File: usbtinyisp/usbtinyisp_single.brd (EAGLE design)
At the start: 44 x 36 mm, 27 parts, among them IC1 ATTINY2313-20P, IC2 74LVX125D, Q1 12000

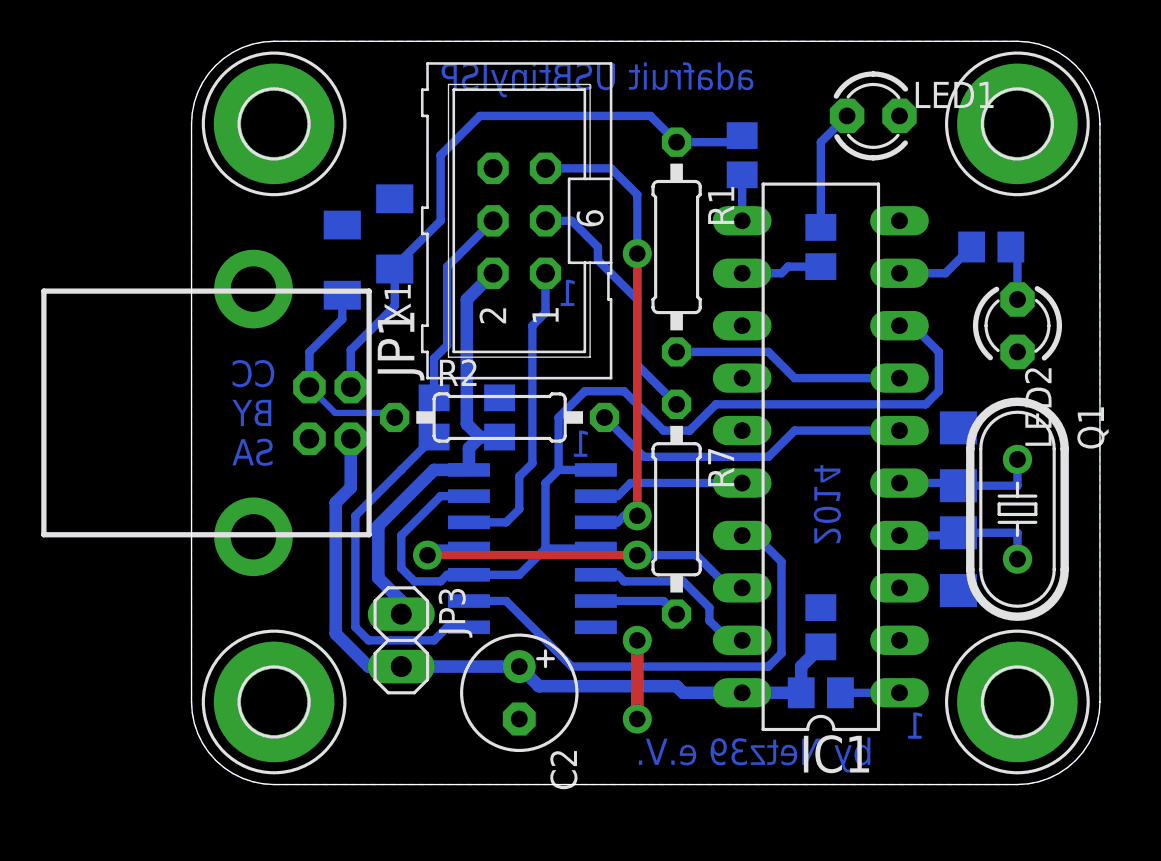
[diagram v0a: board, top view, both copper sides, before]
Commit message: add fuse and diode and route again the whole board
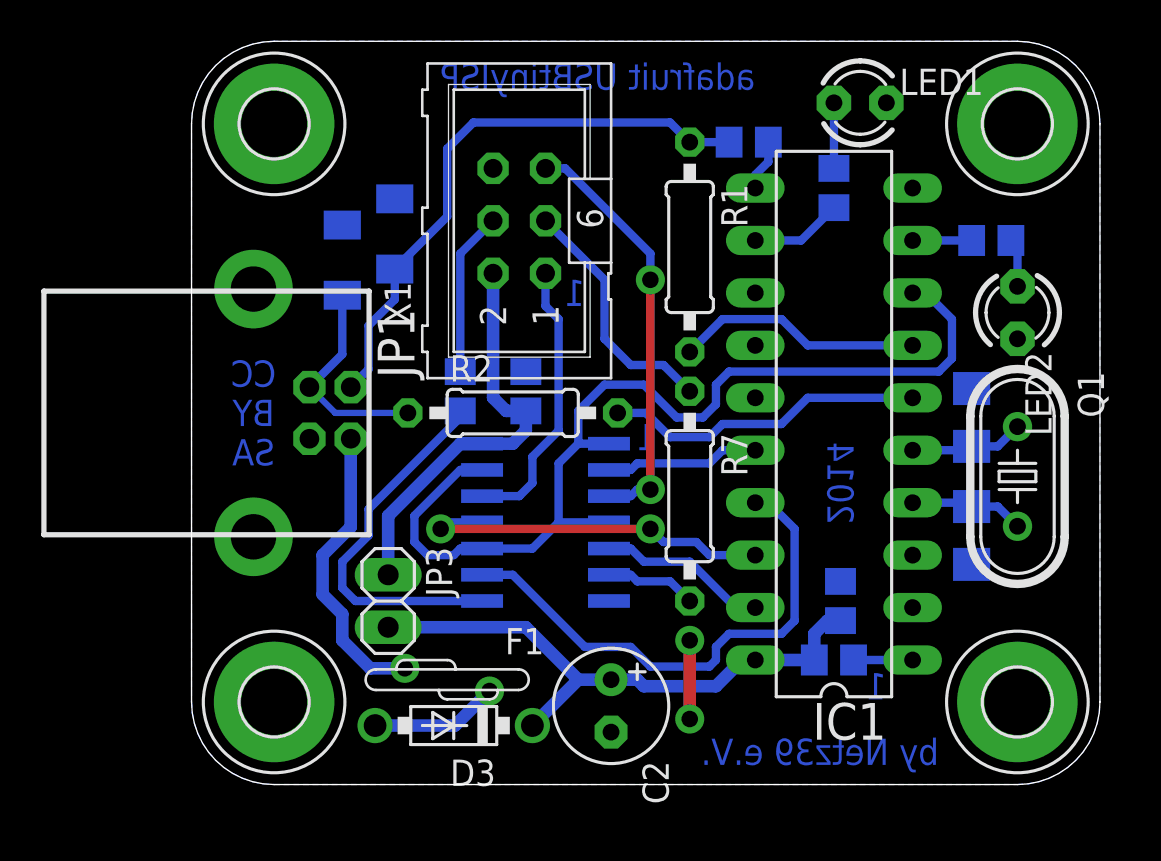
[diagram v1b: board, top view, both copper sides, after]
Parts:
- added D3: 1N5818-B, diode:DO41-7.6
- added F1: (no value), n39:LP60-050
- moved C2 4.49 mm to (20.3, 3.81)
- moved R6 2.93 mm to (31.1, 28.9)
- moved C4 2.01 mm to (37.8, 17.8)
- moved JP3 2.01 mm to (9.53, 8.89)
- moved C5 1.80 mm to (16.2, 19.1)
- moved R4 1.80 mm to (13.0, 19.1)
- moved R10 1.71 mm to (31.1, 6.03)
- moved IC1 1.71 mm to (31.1, 17.5)
- moved C1 1.59 mm to (31.4, 8.89)
- moved Q1 1.59 mm to (40.0, 14.9)
- moved C3 1.42 mm to (37.8, 12.1)
- moved IC2 1.42 mm to (17.1, 12.7)
- moved LED1 0.90 mm to (32.4, 33.0)
- moved R7 0.90 mm to (24.1, 14.0)
- moved R3 0.71 mm to (27.0, 31.1), turned to 180 degrees
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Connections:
- new net N$14: D3.A, F1.P$1
- new net VBUS: F1.P$2, X1.1
- net VCC: now also D3.C; no longer X1.1
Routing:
- net VBUS: track 0.00 -> 14.3 mm
- net VCC: track 36.1 -> 28.3 mm
- net N$14: track 0.00 -> 6.24 mm
- net N$5: track 5.93 -> 3.18 mm
- net RST: track 22.7 -> 20.4 mm
- net MOSI: track 9.76 -> 7.96 mm
- net VTARGET: track 21.7 -> 20.1 mm
- net MOSI': track 23.6 -> 25.1 mm
- net XTAL2: track 7.04 -> 5.55 mm
- net XTAL1: track 7.04 -> 5.55 mm
- net N$1: track 29.2 -> 28.1 mm
- net N$13: track 16.8 -> 18.0 mm
- net N$10: track 4.02 -> 2.86 mm
- net MISO: track 14.7 -> 13.7 mm
- net N$15: track 49.3 -> 48.4 mm
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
